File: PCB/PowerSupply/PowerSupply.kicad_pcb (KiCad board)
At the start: 2 copper layers, 34.2 x 34.2 mm, 21 parts, among them J1 Conn_01x03, U1 PinHeader, U2 Tactile-Switch, U3 Tactile-Switch, U4 ESP32-C6-MINI-1-N4, U5 BidirectionalLogicLevelShifter, U6 LinearVoltageRegulator, U7 USB-TypeC, U8 BidirectionalLogicLevelShifter

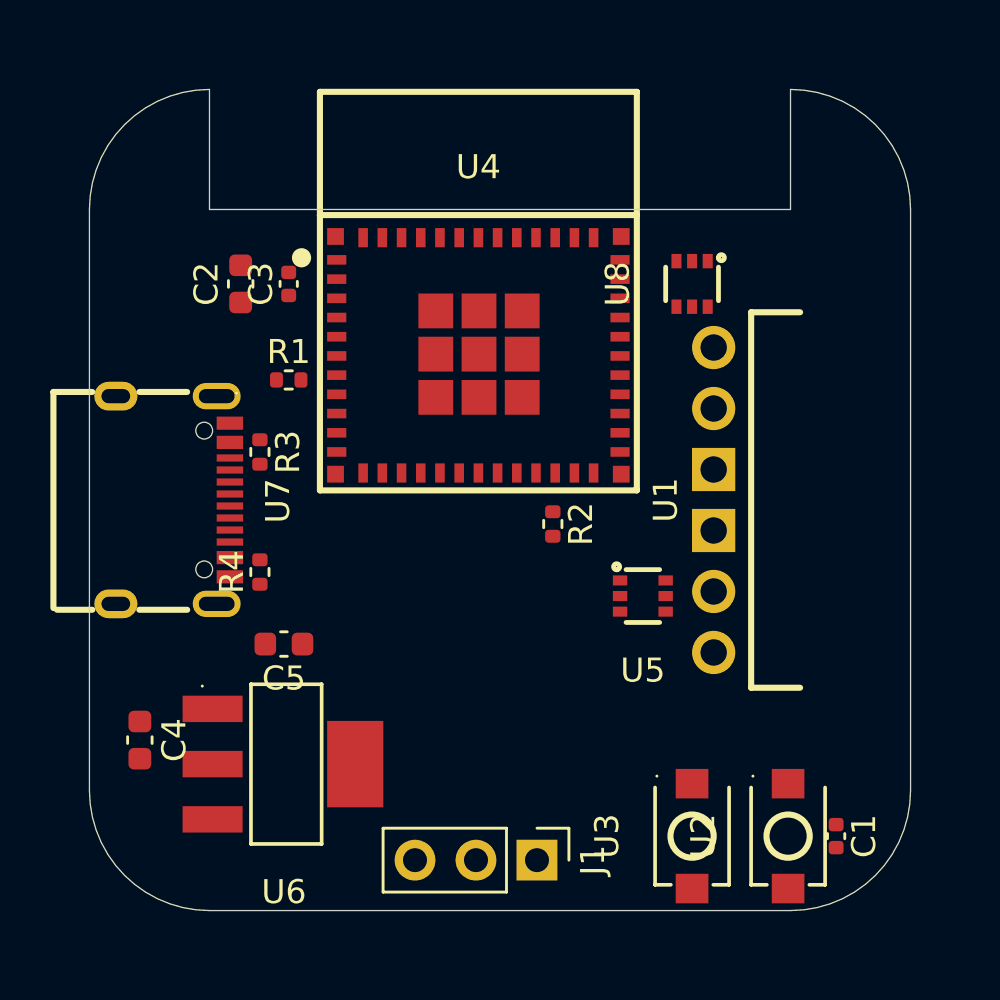
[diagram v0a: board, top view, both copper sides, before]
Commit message: Finish module, power supply and connector design, panel is wip
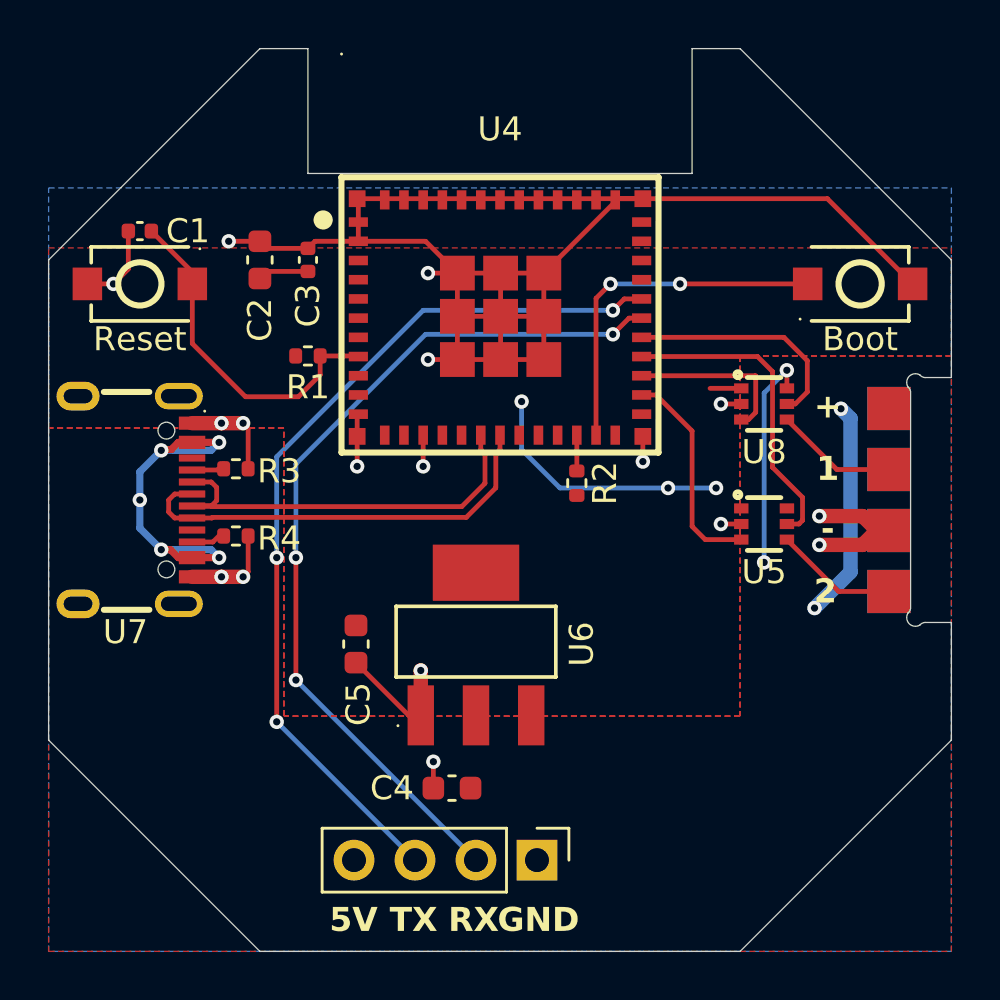
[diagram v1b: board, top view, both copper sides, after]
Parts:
- removed the REF** at (150.9, 90.0)
- removed the REF** at (114.9, 90.0)
- removed the REF** at (132.9, 108.0)
- removed U1: PinHeader, CustomFootprints:01x06_PinHeader_Angled
- added REF**: Tab, PCM_kikit:Tab, F.Cu at (117.9, 105.0)
- added REF**: Tab, PCM_kikit:Tab, F.Cu at (147.9, 105.0)
- added REF**: Tab, PCM_kikit:Tab, F.Cu at (117.9, 75.0)
- added REF**: Tab, PCM_kikit:Tab, F.Cu at (147.9, 75.0)
- added U9: PinHeaderRight, CustomFootprints:01x04_PinPads, F.Cu at (149.1, 90.0)
- C5: value 10uF tantalum or low esr ceramic -> 10uF
- J1: footprint Connector_PinHeader_2.54mm:PinHeader_1x03_P2.54mm_Vertical -> Connector_PinHeader_2.54mm:PinHeader_1x04_P2.54mm_Vertical
- moved C1 38.4 mm to (117.9, 78.8), turned to 180 degrees
- moved U2 35.5 mm to (117.9, 81.0), turned to 0 degrees
- moved U3 24.0 mm to (147.9, 81.0), turned to 180 degrees
- moved C4 13.2 mm to (130.9, 102.0), turned to 0 degrees
- moved U6 9.43 mm to (131.9, 96.0), turned to -90 degrees
- moved U5 5.87 mm to (143.9, 91.0)
- moved U8 5.83 mm to (143.9, 86.0), turned to 180 degrees
- moved C5 3.00 mm to (126.9, 96.0), turned to -90 degrees
- moved R2 1.97 mm to (136.1, 89.3)
- moved U4 1.81 mm to (132.9, 82.4)
- moved R4 1.80 mm to (121.9, 91.5), turned to 180 degrees
- moved U7 1.58 mm to (117.7, 90.0)
- moved C2 1.28 mm to (122.9, 80.0)
- moved C3 1.28 mm to (124.9, 80.0)
- moved R1 1.28 mm to (124.9, 84.0)
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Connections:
- C2 pad 1: +3V3 -> +3.3V
- C3 pad 1: +3V3 -> +3.3V
- J1 pad 1: TX -> GND
- J1 pad 3: GND -> TX
- R1 pad 1: +3V3 -> +3.3V
- R2 pad 2: +3V3 -> +3.3V
- U4 pad 10: DIR2 -> unconnected-(U4-IO5-Pad10)
- U4 pad 26: unconnected-(U4-IO20-Pad26) -> /DataTop1_3V3
- U4 pad 27: unconnected-(U4-IO21-Pad27) -> /DataTop2_3V3
- U4 pad 28: unconnected-(U4-IO22-Pad28) -> DIR1
- U4 pad 29: unconnected-(U4-IO23-Pad29) -> DIR2
- U4 pad 5: /DataTop2_3V3 -> unconnected-(U4-IO2-Pad5)
- U4 pad 6: /DataTop1_3V3 -> unconnected-(U4-IO3-Pad6)
- U4 pad 9: DIR1 -> unconnected-(U4-IO4-Pad9)
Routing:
- net GND: track 0.00 -> 95.5 mm, vias 0 -> 17
- net TX: track 0.00 -> 37.1 mm, vias 0 -> 3
- net RX: track 0.00 -> 36.5 mm, vias 0 -> 3
- net +5V: track 0.00 -> 33.3 mm, vias 0 -> 9
- net USB_D+: track 0.00 -> 18.1 mm
- net USB_D-: track 0.00 -> 17.5 mm
- net EN: track 0.00 -> 14.8 mm
- net IO9: track 0.00 -> 14.8 mm, vias 0 -> 2
- net +3.3V: track 0.00 -> 14.2 mm, vias 0 -> 3
- net DIR1: track 0.00 -> 13.1 mm
- net DIR2: track 0.00 -> 9.66 mm
- net /DataTop1_3V3: track 0.00 -> 8.97 mm
- net /DataTop2_3V3: track 0.00 -> 6.99 mm
- net /DataTop1_5V: track 0.00 -> 5.14 mm
- net /DataTop2_5V: track 0.00 -> 5.11 mm
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- added copper zone on F.Cu, net +3.3V
- added copper zone on F.Cu, net +5V
- added copper zone on B.Cu, net GND
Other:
- board size 34.2 x 34.2 mm -> 37.6 x 37.6 mm
- board text added: "+"
- board text added: "-"
- board text added: "1"
- board text added: "2"
- board text added: "5V"
- board text added: "Boot"
- board text added: "D1"
- board text added: "D2"
- board text added: "GND"
- board text added: "Pogo"
- board text added: "RX"
- board text added: "Reset"
- board text added: "TX"

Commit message: Finish panel script
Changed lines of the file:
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@@
 			(at 0 -2 180)
 			(layer "F.SilkS")
+			(hide yes)
 			(effects
 				(font
@@
 			(at 2.5 -0.1 90)
 			(layer "F.SilkS")
+			(hide yes)
 			(effects
 				(font
@@
 			(at -2.5 0 90)
 			(layer "F.SilkS")
+			(hide yes)
 			(effects
 				(font
@@
 		(tags "capacitor")
 		(property "Reference" "C4"
-			(at -2.5 0 360)
+			(at -2.5 0 0)
 			(layer "F.SilkS")
+			(hide yes)
 			(effects
 				(font
@@
 		)
 		(property "Value" "10uF"
-			(at 0 1.43 360)
+			(at 0 1.43 0)
 			(layer "F.Fab")
 			(effects
@@
 		)
 		(fp_text user "${REFERENCE}"
-			(at 0 0 360)
+			(at 0 0 0)
 			(layer "F.Fab")
 			(effects
@@
 			(at -0.000013 -4.4 90)
 			(layer "F.SilkS")
+			(hide yes)
 			(effects
 				(font
@@
 		(tags "resistor")
 		(property "Reference" "R4"
-			(at -1.8 -0.1 360)
+			(at -1.8 -0.1 0)
 			(layer "F.SilkS")
+			(hide yes)
 			(effects
 				(font
@@
 		)
 		(property "Value" "5k1"
-			(at 0 1.17 360)
+			(at 0 1.17 0)
 			(layer "F.Fab")
 			(effects
@@
 		)
 		(fp_text user "${REFERENCE}"
-			(at 0 0 360)
+			(at 0 0 0)
 			(layer "F.Fab")
 			(effects
@@
 			(at 5.5 0.4 180)
 			(layer "F.SilkS")
+			(hide yes)
 			(effects
 				(font
@@
 			(at 0 -1.17 90)
 			(layer "F.SilkS")
+			(hide yes)
 			(effects
 				(font
@@
 		(tags "SC-70-6_L2.2-W1.3-P0.65-LS2.1-BR footprint C168855")
 		(property "Reference" "U8"
-			(at 0 -2 360)
+			(at 0 -2 0)
 			(layer "F.SilkS")
+			(hide yes)
 			(effects
 				(font
@@
 		)
 		(property "Value" "BidirectionalLogicLevelShifter"
-			(at 0 3.1 360)
+			(at 0 3.1 0)
 			(layer "F.Fab")
 			(effects
@@
 		)
 		(property "Footprint" "CustomFootprints:BidirectionalLogicLevelConverter"
-			(at 0 0 360)
+			(at 0 0 0)
 			(layer "F.Fab")
 			(hide yes)
@@
 		)
 		(property "Datasheet" "https://item.szlcsc.com/112963.html"
-			(at 0 0 360)
+			(at 0 0 0)
 			(layer "F.Fab")
 			(hide yes)
@@
 		)
 		(property "Description" ""
-			(at 0 0 360)
+			(at 0 0 0)
 			(layer "F.Fab")
 			(hide yes)
@@
 		)
 		(fp_text user "REF**"
-			(at 0 5.1 360)
+			(at 0 5.1 0)
 			(layer "F.Fab")
 			(effects
@@
 		)
 		(fp_text user "KIKIT: width: 5mm"
-			(at -5.5 0 225)
+			(at -5.5 0 -135)
 			(layer "Dwgs.User")
 			(effects
@@
 			(at -1.9 0 90)
 			(layer "F.SilkS")
+			(hide yes)
 			(effects
 				(font
@@
 			(at 0 1.3 0)
 			(layer "F.SilkS")
+			(hide yes)
 			(effects
 				(font
@@
 		)
 		(property "Value" "Tactile-Switch"
-			(at 0 3.541199 360)
+			(at 0 3.541199 0)
 			(layer "F.Fab")
 			(effects
@@
 		)
 		(property "Footprint" "CustomFootprints:Button"
-			(at 0 0 360)
+			(at 0 0 0)
 			(layer "F.Fab")
 			(hide yes)
@@
 		)
 		(property "Datasheet" "https://item.szlcsc.com/457636.html"
-			(at 0 0 360)
+			(at 0 0 0)
 			(layer "F.Fab")
 			(hide yes)
@@
 		)
 		(property "Description" ""
-			(at 0 0 360)
+			(at 0 0 0)
 			(layer "F.Fab")
 			(hide yes)
@@
 		)
 		(fp_text user "REF**"
-			(at 0 5.541199 360)
+			(at 0 5.541199 0)
 			(layer "F.Fab")
 			(effects
@@
 		(tags "capacitor")
 		(property "Reference" "C1"
-			(at -2 0 360)
+			(at -2 0 0)
 			(layer "F.SilkS")
+			(hide yes)
 			(effects
 				(font
@@
 		)
 		(property "Value" "100nF-Ceramic"
-			(at 0 1.16 360)
+			(at 0 1.16 0)
 			(layer "F.Fab")
 			(effects
@@
 		)
 		(fp_text user "${REFERENCE}"
-			(at 0 0 360)
+			(at 0 0 0)
 			(layer "F.Fab")
 			(effects
@@
 		)
 		(fp_text user "KIKIT: width: 5mm"
-			(at -5.5 0 315)
+			(at -5.5 0 -45)
 			(layer "Dwgs.User")
 			(effects
@@
 			(at 0 -7.841986 0)
 			(layer "F.SilkS")
+			(hide yes)
 			(effects
 				(font
@@
 		(tags "resistor")
 		(property "Reference" "R3"
-			(at -1.8 -0.1 360)
+			(at -1.8 -0.1 0)
 			(layer "F.SilkS")
+			(hide yes)
 			(effects
 				(font
@@
 		)
 		(property "Value" "5k1"
-			(at 0 1.17 360)
+			(at 0 1.17 0)
 			(layer "F.Fab")
 			(effects
@@
 		)
 		(fp_text user "${REFERENCE}"
-			(at 0 0 360)
+			(at 0 0 0)
 			(layer "F.Fab")
 			(effects
@@
 		)
 		(property "Value" "Tactile-Switch"
-			(at 0 3.541199 360)
+			(at 0 3.541199 0)
 			(layer "F.Fab")
 			(effects
@@
 		)
 		(property "Footprint" "CustomFootprints:Button"
-			(at 0 0 360)
+			(at 0 0 0)
 			(layer "F.Fab")
 			(hide yes)
@@
 		)
 		(property "Datasheet" "https://item.szlcsc.com/457636.html"
-			(at 0 0 360)
+			(at 0 0 0)
 			(layer "F.Fab")
 			(hide yes)
@@
 		)
 		(property "Description" ""
-			(at 0 0 360)
+			(at 0 0 0)
 			(layer "F.Fab")
 			(hide yes)
@@
 		)
 		(fp_text user "REF**"
-			(at 0 5.541199 360)
+			(at 0 5.541199 0)
 			(layer "F.Fab")
 			(effects

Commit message: Add electrolytic bulk capacitors to modules and power supply
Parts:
- added C6: ElectrolyticCapacitorSMD, CustomFootprints:CAP-SMD_BD6.3-L6.6-W6.6-FD, F.Cu at (139.9, 95.0)
- added C7: ElectrolyticCapacitorSMD, CustomFootprints:CAP-SMD_BD6.3-L6.6-W6.6-FD, F.Cu at (139.9, 102.0)
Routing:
- net GND: track 95.5 -> 98.9 mm, vias 17 -> 19
